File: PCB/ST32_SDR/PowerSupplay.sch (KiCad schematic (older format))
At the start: 30 parts, among them J5 USB_B_Mini, U4 AP1117-33, U5 MC34063, U6 MC34063, U7 78M09

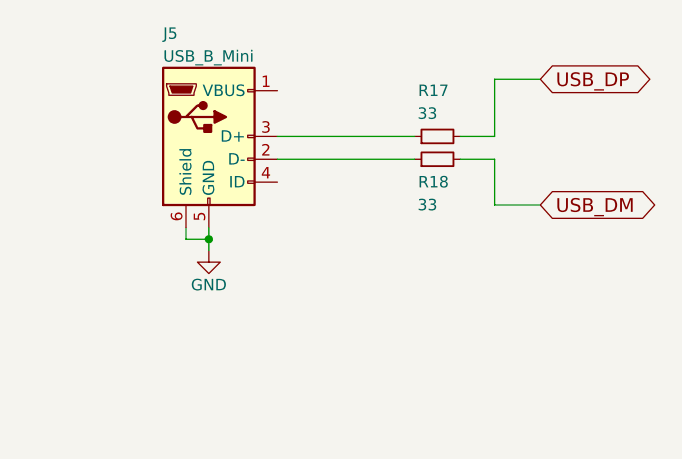
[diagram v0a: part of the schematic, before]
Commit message: PCB Linux 2, update AUDIO_OUT
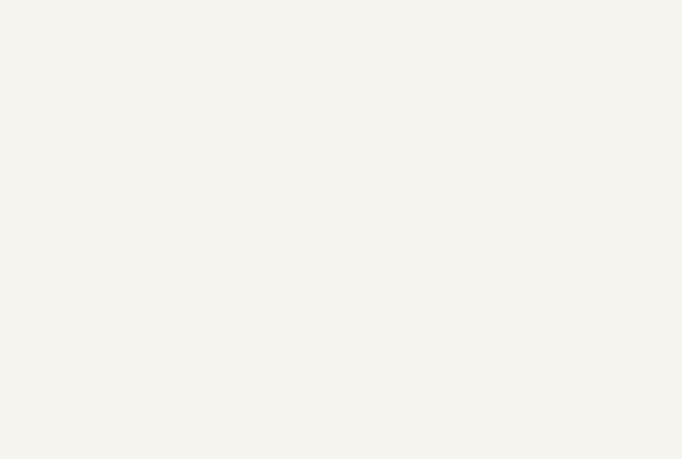
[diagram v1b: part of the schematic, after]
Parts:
- removed J5: USB_B_Mini, Connect:USB_Mini-B, symbol USB_B_Mini
- removed R17, R18: 33, UI:R_1206_0603, symbol R_Small
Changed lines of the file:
@@
 LIBS:4ms-ic
 LIBS:Display
-LIBS:switches
-LIBS:cmos4000
+LIBS:Connector
+LIBS:Relay
 LIBS:LCSDR-cache
 EELAYER 25 0
@@
 Connection ~ 2100 2400
 $Comp
-L GND #PWR083
+L GND #PWR084
 U 1 1 5DD9A087
 P 4600 1900
-F 0 "#PWR083" H 4600 1650 50  0001 C CNN
+F 0 "#PWR084" H 4600 1650 50  0001 C CNN
 F 1 "GND" H 4600 1750 50  0001 C CNN
 F 2 "" H 4600 1900 50  0001 C CNN
@@
 Connection ~ 3950 2400
 $Comp
-L GND #PWR084
+L GND #PWR085
 U 1 1 5DD9A371
 P 3600 2250
-F 0 "#PWR084" H 3600 2000 50  0001 C CNN
+F 0 "#PWR085" H 3600 2000 50  0001 C CNN
 F 1 "GND" H 3600 2100 50  0001 C CNN
 F 2 "" H 3600 2250 50  0001 C CNN
@@
 $EndComp
 $Comp
-L GND #PWR085
+L GND #PWR086
 U 1 1 5DD9A42B
 P 3400 2150
-F 0 "#PWR085" H 3400 1900 50  0001 C CNN
+F 0 "#PWR086" H 3400 1900 50  0001 C CNN
 F 1 "GND" H 3400 2000 50  0001 C CNN
 F 2 "" H 3400 2150 50  0001 C CNN
@@
 Connection ~ 2150 1350
 $Comp
-L +12V #PWR086
+L +12V #PWR087
 U 1 1 5DD9A4E4
 P 1250 2000
-F 0 "#PWR086" H 1250 1850 50  0001 C CNN
+F 0 "#PWR087" H 1250 1850 50  0001 C CNN
 F 1 "+12V" V 1250 2250 50  0000 C CNN
 F 2 "" H 1250 2000 50  0001 C CNN
@@
 Connection ~ 4150 2400
 $Comp
-L +12V #PWR087
+L +12V #PWR088
 U 1 1 5DD9C169
 P 2700 3250
-F 0 "#PWR087" H 2700 3100 50  0001 C CNN
+F 0 "#PWR088" H 2700 3100 50  0001 C CNN
 F 1 "+12V" V 2700 3500 50  0000 C CNN
 F 2 "" H 2700 3250 50  0001 C CNN
@@
 $EndComp
 $Comp
-L +9V #PWR088
+L +9V #PWR089
 U 1 1 5DD9C2C5
 P 4400 2400
-F 0 "#PWR088" H 4400 2250 50  0001 C CNN
+F 0 "#PWR089" H 4400 2250 50  0001 C CNN
 F 1 "+9V" V 4400 2600 50  0000 C CNN
 F 2 "" H 4400 2400 50  0001 C CNN
@@
 $EndComp
 $Comp
-L +9V #PWR089
+L +9V #PWR090
 U 1 1 5DD9C3E9
 P 3300 3250
-F 0 "#PWR089" H 3300 3100 50  0001 C CNN
+F 0 "#PWR090" H 3300 3100 50  0001 C CNN
 F 1 "+9V" V 3300 3450 50  0000 C CNN
 F 2 "" H 3300 3250 50  0001 C CNN
@@
 $EndComp
 $Comp
-L GND #PWR090
+L GND #PWR091
 U 1 1 5DD9C454
 P 3000 3550
-F 0 "#PWR090" H 3000 3300 50  0001 C CNN
+F 0 "#PWR091" H 3000 3300 50  0001 C CNN
 F 1 "GND" H 3000 3400 50  0001 C CNN
 F 2 "" H 3000 3550 50  0001 C CNN
@@
 $EndComp
 $Comp
-L GND #PWR091
+L GND #PWR092
 U 1 1 5DD9C4CE
 P 3250 2650
-F 0 "#PWR091" H 3250 2400 50  0001 C CNN
+F 0 "#PWR092" H 3250 2400 50  0001 C CNN
 F 1 "GND" H 3250 2500 50  0001 C CNN
 F 2 "" H 3250 2650 50  0001 C CNN
@@
 $EndComp
 $Comp
-L GND #PWR092
+L GND #PWR093
 U 1 1 5DD9C50C
 P 3950 2650
-F 0 "#PWR092" H 3950 2400 50  0001 C CNN
+F 0 "#PWR093" H 3950 2400 50  0001 C CNN
 F 1 "GND" H 3950 2500 50  0001 C CNN
 F 2 "" H 3950 2650 50  0001 C CNN
@@
 $EndComp
 $Comp
-L GND #PWR093
+L GND #PWR094
 U 1 1 5DD9C54A
 P 2100 2650
-F 0 "#PWR093" H 2100 2400 50  0001 C CNN
+F 0 "#PWR094" H 2100 2400 50  0001 C CNN
 F 1 "GND" H 2100 2500 50  0001 C CNN
 F 2 "" H 2100 2650 50  0001 C CNN
@@
 $EndComp
 $Comp
-L GND #PWR094
+L GND #PWR095
 U 1 1 5DD9C5AC
 P 1650 2300
-F 0 "#PWR094" H 1650 2050 50  0001 C CNN
+F 0 "#PWR095" H 1650 2050 50  0001 C CNN
 F 1 "GND" H 1650 2150 50  0001 C CNN
 F 2 "" H 1650 2300 50  0001 C CNN
@@
 Connection ~ 2050 4950
 $Comp
-L GND #PWR095
+L GND #PWR096
 U 1 1 5DD9C919
 P 4550 4450
-F 0 "#PWR095" H 4550 4200 50  0001 C CNN
+F 0 "#PWR096" H 4550 4200 50  0001 C CNN
 F 1 "GND" H 4550 4300 50  0001 C CNN
 F 2 "" H 4550 4450 50  0001 C CNN
@@
 Connection ~ 3900 4950
 $Comp
-L GND #PWR096
+L GND #PWR097
 U 1 1 5DD9C936
 P 3550 4800
-F 0 "#PWR096" H 3550 4550 50  0001 C CNN
+F 0 "#PWR097" H 3550 4550 50  0001 C CNN
 F 1 "GND" H 3550 4650 50  0001 C CNN
 F 2 "" H 3550 4800 50  0001 C CNN
@@
 $EndComp
 $Comp
-L GND #PWR097
+L GND #PWR098
 U 1 1 5DD9C93C
 P 3350 4700
-F 0 "#PWR097" H 3350 4450 50  0001 C CNN
+F 0 "#PWR098" H 3350 4450 50  0001 C CNN
 F 1 "GND" H 3350 4550 50  0001 C CNN
 F 2 "" H 3350 4700 50  0001 C CNN
@@
 Connection ~ 4100 4950
 $Comp
-L GND #PWR098
+L GND #PWR099
 U 1 1 5DD9C97A
 P 2550 5900
-F 0 "#PWR098" H 2550 5650 50  0001 C CNN
+F 0 "#PWR099" H 2550 5650 50  0001 C CNN
 F 1 "GND" H 2550 5750 50  0001 C CNN
 F 2 "" H 2550 5900 50  0001 C CNN
@@
 $EndComp
 $Comp
-L GND #PWR099
+L GND #PWR0100
 U 1 1 5DD9C980
 P 3200 5200
-F 0 "#PWR099" H 3200 4950 50  0001 C CNN
+F 0 "#PWR0100" H 3200 4950 50  0001 C CNN
 F 1 "GND" H 3200 5050 50  0001 C CNN
 F 2 "" H 3200 5200 50  0001 C CNN
@@
 $EndComp
 $Comp
-L GND #PWR0100
+L GND #PWR0101
 U 1 1 5DD9C986
 P 3900 5200
-F 0 "#PWR0100" H 3900 4950 50  0001 C CNN
+F 0 "#PWR0101" H 3900 4950 50  0001 C CNN
 F 1 "GND" H 3900 5050 50  0001 C CNN
 F 2 "" H 3900 5200 50  0001 C CNN
@@
 $EndComp
 $Comp
-L GND #PWR0101
+L GND #PWR0102
 U 1 1 5DD9C98C
 P 2050 5200
-F 0 "#PWR0101" H 2050 4950 50  0001 C CNN
+F 0 "#PWR0102" H 2050 4950 50  0001 C CNN
 F 1 "GND" H 2050 5050 50  0001 C CNN
 F 2 "" H 2050 5200 50  0001 C CNN
@@
 $EndComp
 $Comp
-L GND #PWR0102
+L GND #PWR0103
 U 1 1 5DD9C992
 P 1600 4850
-F 0 "#PWR0102" H 1600 4600 50  0001 C CNN
+F 0 "#PWR0103" H 1600 4600 50  0001 C CNN
 F 1 "GND" H 1600 4700 50  0001 C CNN
 F 2 "" H 1600 4850 50  0001 C CNN
@@
 $EndComp
 $Comp
-L +9V #PWR0103
+L +9V #PWR0104
 U 1 1 5DD9CCE8
 P 1400 4550
-F 0 "#PWR0103" H 1400 4400 50  0001 C CNN
+F 0 "#PWR0104" H 1400 4400 50  0001 C CNN
 F 1 "+9V" V 1400 4750 50  0000 C CNN
 F 2 "" H 1400 4550 50  0001 C CNN
@@
 $EndComp
 $Comp
-L +3.3V #PWR0104
+L +3.3V #PWR0105
 U 1 1 5DD9CE73
 P 4350 4950
-F 0 "#PWR0104" H 4350 4800 50  0001 C CNN
+F 0 "#PWR0105" H 4350 4800 50  0001 C CNN
 F 1 "+3.3V" V 4350 5200 50  0000 C CNN
 F 2 "" H 4350 4950 50  0001 C CNN
@@
 $EndComp
 $Comp
-L +3.3V #PWR0105
+L +3.3V #PWR0106
 U 1 1 5DD9D384
 P 2850 5600
-F 0 "#PWR0105" H 2850 5450 50  0001 C CNN
+F 0 "#PWR0106" H 2850 5450 50  0001 C CNN
 F 1 "+3.3V" V 2850 5850 50  0000 C CNN
 F 2 "" H 2850 5600 50  0001 C CNN
@@
 $EndComp
 $Comp
-L +3.3V #PWR0106
+L +3.3V #PWR0107
 U 1 1 5DDE4F01
 P 5700 4950
-F 0 "#PWR0106" H 5700 4800 50  0001 C CNN
+F 0 "#PWR0107" H 5700 4800 50  0001 C CNN
 F 1 "+3.3V" V 5700 5200 50  0000 C CNN
 F 2 "" H 5700 4950 50  0001 C CNN
@@
 	5700 4950 5850 4950
 $Comp
-L +3V3 #PWR0107
+L +3V3 #PWR0108
 U 1 1 5DDE50CB
 P 6800 4950
-F 0 "#PWR0107" H 6800 4800 50  0001 C CNN
+F 0 "#PWR0108" H 6800 4800 50  0001 C CNN
 F 1 "+3V3" V 6800 5200 50  0000 C CNN
 F 2 "" H 6800 4950 50  0001 C CNN
@@
 $EndComp
 $Comp
-L GND #PWR0108
+L GND #PWR0109
 U 1 1 5DDE5565
 P 6200 5200
-F 0 "#PWR0108" H 6200 4950 50  0001 C CNN
+F 0 "#PWR0109" H 6200 4950 50  0001 C CNN
 F 1 "GND" H 6200 5050 50  0001 C CNN
 F 2 "" H 6200 5200 50  0001 C CNN
@@
 $EndComp
 $Comp
-L GND #PWR0109
+L GND #PWR0110
 U 1 1 5DDE5612
 P 6700 5200
-F 0 "#PWR0109" H 6700 4950 50  0001 C CNN
+F 0 "#PWR0110" H 6700 4950 50  0001 C CNN
 F 1 "GND" H 6700 5050 50  0001 C CNN
 F 2 "" H 6700 5200 50  0001 C CNN
@@
 $EndComp
 $Comp
-L USB_B_Mini J5
-U 1 1 5DDFB4C7
-P 8500 1850
-F 0 "J5" H 8300 2300 50  0000 L CNN
-F 1 "USB_B_Mini" H 8300 2200 50  0000 L CNN
-F 2 "Connect:USB_Mini-B" H 8650 1800 50  0001 C CNN
-F 3 "" H 8650 1800 50  0001 C CNN
-	1    8500 1850
-	1    0    0    -1
-$EndComp
-$Comp
-L R_Small R17
-U 1 1 5DDFB6BD
-P 9500 1850
-F 0 "R17" V 9700 1800 50  0000 L CNN
-F 1 "33" V 9200 1850 50  0000 L CNN
-F 2 "UI:R_1206_0603" H 9500 1850 50  0001 C CNN
-F 3 "" H 9500 1850 50  0001 C CNN
-	1    9500 1850
-	0    -1   -1   0
-$EndComp
-Wire Wire Line
-	9400 1850 8800 1850
-Wire Wire Line
-	8800 1950 9400 1950
-$Comp
-L R_Small R18
-U 1 1 5DDFB8C3
-P 9500 1950
-F 0 "R18" V 9400 1900 50  0000 L CNN
-F 1 "33" V 9700 1950 50  0000 L CNN
-F 2 "UI:R_1206_0603" H 9500 1950 50  0001 C CNN
-F 3 "" H 9500 1950 50  0001 C CNN
-	1    9500 1950
-	0    -1   -1   0
-$EndComp
-Wire Wire Line
-	9600 1850 9750 1850
-Wire Wire Line
-	9750 1850 9750 1600
-Wire Wire Line
-	9750 1600 9950 1600
-Wire Wire Line
-	9600 1950 9750 1950
-Wire Wire Line
-	9750 1950 9750 2150
-Wire Wire Line
-	9750 2150 9950 2150
-Text GLabel 9950 2150 2    60   BiDi ~ 0
-USB_DM
-Text GLabel 9950 1600 2    60   BiDi ~ 0
-USB_DP
-$Comp
-L GND #PWR0110
-U 1 1 5DDFC12C
-P 8500 2350
-F 0 "#PWR0110" H 8500 2100 50  0001 C CNN
-F 1 "GND" H 8500 2200 50  0000 C CNN
-F 2 "" H 8500 2350 50  0001 C CNN
-F 3 "" H 8500 2350 50  0001 C CNN
-	1    8500 2350
-	1    0    0    -1
-$EndComp
-Wire Wire Line
-	8400 2250 8400 2300
-Wire Wire Line
-	8400 2300 8500 2300
-Wire Wire Line
-	8500 2250 8500 2350
-Connection ~ 8500 2300
-$Comp
 L +9V #PWR0111
